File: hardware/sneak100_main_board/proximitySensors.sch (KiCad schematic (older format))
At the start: 4 parts, among them J11 Conn_01x03, J12 Conn_01x03, J13 Conn_01x03, J14 Conn_01x03

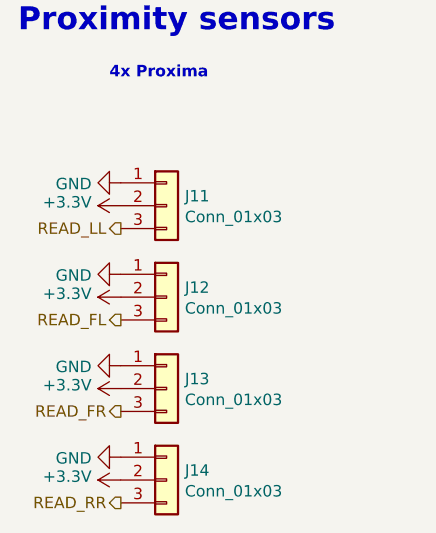
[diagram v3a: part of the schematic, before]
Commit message: proximity sensors connectors
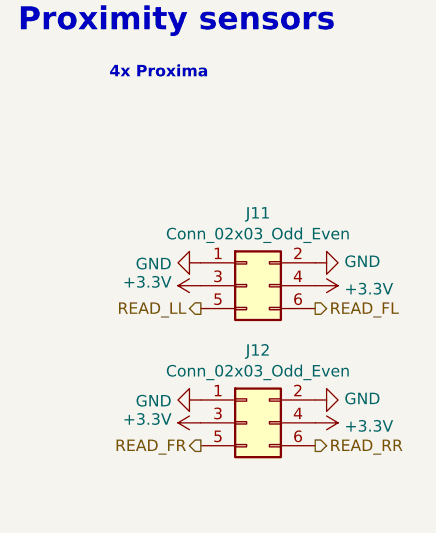
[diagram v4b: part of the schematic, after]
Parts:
- removed J11, J12, J13, J14: Conn_01x03, Connector_PinHeader_2.54mm:PinHeader_1x03_P2.54mm_Vertical, symbol Connector_Generic:Conn_01x03
- added J11, J12: Conn_02x03_Odd_Even, Connector_PinSocket_2.54mm:PinSocket_2x03_P2.54mm_Horizontal, symbol Connector_Generic:Conn_02x03_Odd_Even
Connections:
- net +3V3: now also J11.3 (Pin_3), J11.4 (Pin_4), J12.3 (Pin_3), J12.4 (Pin_4)
- net GND: now also J11.1 (Pin_1), J11.2 (Pin_2), J12.1 (Pin_1), J12.2 (Pin_2)
- net READ_FL: now also J11.6 (Pin_6)
- net READ_FR: now also J12.5 (Pin_5)
- net READ_LL: now also J11.5 (Pin_5)
- net READ_RR: now also J12.6 (Pin_6)
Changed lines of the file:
@@
 $EndDescr
-$Comp
-L Connector_Generic:Conn_01x03 J?
-U 1 1 610BA2A4
-P 5050 3200
-AR Path="/60E04A74/610BA2A4" Ref="J?"  Part="1"
-AR Path="/60E049FE/610BA2A4" Ref="J11"  Part="1"
-F 0 "J11" H 5130 3242 50  0000 L CNN
-F 1 "Conn_01x03" H 5130 3151 50  0000 L CNN
-F 2 "Connector_PinHeader_2.54mm:PinHeader_1x03_P2.54mm_Vertical" H 5050 3200 50  0001 C CNN
-F 3 "~" H 5050 3200 50  0001 C CNN
-	1    5050 3200
-	1    0    0    -1
-$EndComp
-$Comp
-L Connector_Generic:Conn_01x03 J?
-U 1 1 610BA2AA
-P 5050 3600
-AR Path="/60E04A74/610BA2AA" Ref="J?"  Part="1"
-AR Path="/60E049FE/610BA2AA" Ref="J12"  Part="1"
-F 0 "J12" H 5130 3642 50  0000 L CNN
-F 1 "Conn_01x03" H 5130 3551 50  0000 L CNN
-F 2 "Connector_PinHeader_2.54mm:PinHeader_1x03_P2.54mm_Vertical" H 5050 3600 50  0001 C CNN
-F 3 "~" H 5050 3600 50  0001 C CNN
-	1    5050 3600
-	1    0    0    -1
-$EndComp
-$Comp
-L Connector_Generic:Conn_01x03 J?
-U 1 1 610BA2B0
-P 5050 4000
-AR Path="/60E04A74/610BA2B0" Ref="J?"  Part="1"
-AR Path="/60E049FE/610BA2B0" Ref="J13"  Part="1"
-F 0 "J13" H 5130 4042 50  0000 L CNN
-F 1 "Conn_01x03" H 5130 3951 50  0000 L CNN
-F 2 "Connector_PinHeader_2.54mm:PinHeader_1x03_P2.54mm_Vertical" H 5050 4000 50  0001 C CNN
-F 3 "~" H 5050 4000 50  0001 C CNN
-	1    5050 4000
-	1    0    0    -1
-$EndComp
-$Comp
-L Connector_Generic:Conn_01x03 J?
-U 1 1 610BA2B6
-P 5050 4400
-AR Path="/60E04A74/610BA2B6" Ref="J?"  Part="1"
-AR Path="/60E049FE/610BA2B6" Ref="J14"  Part="1"
-F 0 "J14" H 5130 4442 50  0000 L CNN
-F 1 "Conn_01x03" H 5130 4351 50  0000 L CNN
-F 2 "Connector_PinHeader_2.54mm:PinHeader_1x03_P2.54mm_Vertical" H 5050 4400 50  0001 C CNN
-F 3 "~" H 5050 4400 50  0001 C CNN
-	1    5050 4400
-	1    0    0    -1
-$EndComp
 $Comp
 L power:+3.3V #PWR?
 U 1 1 610BA2BC
-P 4850 3200
+P 5200 3550
 AR Path="/60E04A74/610BA2BC" Ref="#PWR?"  Part="1"
-AR Path="/60E049FE/610BA2BC" Ref="#PWR080"  Part="1"
-F 0 "#PWR080" H 4850 3050 50  0001 C CNN
-F 1 "+3.3V" V 4865 3328 50  0000 L CNN
-F 2 "" H 4850 3200 50  0001 C CNN
-F 3 "" H 4850 3200 50  0001 C CNN
-	1    4850 3200
+AR Path="/60E049FE/610BA2BC" Ref="#PWR081"  Part="1"
+F 0 "#PWR081" H 5200 3400 50  0001 C CNN
+F 1 "+3.3V" V 5215 3678 50  0000 L CNN
+F 2 "" H 5200 3550 50  0001 C CNN
+F 3 "" H 5200 3550 50  0001 C CNN
+	1    5200 3550
 	0    -1   -1   0
 $EndComp
@@
 L power:+3.3V #PWR?
 U 1 1 610BA2C2
-P 4850 3600
+P 5700 3550
 AR Path="/60E04A74/610BA2C2" Ref="#PWR?"  Part="1"
 AR Path="/60E049FE/610BA2C2" Ref="#PWR082"  Part="1"
-F 0 "#PWR082" H 4850 3450 50  0001 C CNN
-F 1 "+3.3V" V 4865 3728 50  0000 L CNN
-F 2 "" H 4850 3600 50  0001 C CNN
-F 3 "" H 4850 3600 50  0001 C CNN
-	1    4850 3600
-	0    -1   -1   0
+F 0 "#PWR082" H 5700 3400 50  0001 C CNN
+F 1 "+3.3V" V 5715 3678 50  0000 L CNN
+F 2 "" H 5700 3550 50  0001 C CNN
+F 3 "" H 5700 3550 50  0001 C CNN
+	1    5700 3550
+	0    1    1    0
 $EndComp
 $Comp
 L power:+3.3V #PWR?
 U 1 1 610BA2C8
-P 4850 4000
+P 5200 4150
 AR Path="/60E04A74/610BA2C8" Ref="#PWR?"  Part="1"
-AR Path="/60E049FE/610BA2C8" Ref="#PWR084"  Part="1"
-F 0 "#PWR084" H 4850 3850 50  0001 C CNN
-F 1 "+3.3V" V 4865 4128 50  0000 L CNN
-F 2 "" H 4850 4000 50  0001 C CNN
-F 3 "" H 4850 4000 50  0001 C CNN
-	1    4850 4000
+AR Path="/60E049FE/610BA2C8" Ref="#PWR085"  Part="1"
+F 0 "#PWR085" H 5200 4000 50  0001 C CNN
+F 1 "+3.3V" V 5215 4278 50  0000 L CNN
+F 2 "" H 5200 4150 50  0001 C CNN
+F 3 "" H 5200 4150 50  0001 C CNN
+	1    5200 4150
 	0    -1   -1   0
 $EndComp
@@
 L power:+3.3V #PWR?
 U 1 1 610BA2CE
-P 4850 4400
+P 5700 4150
 AR Path="/60E04A74/610BA2CE" Ref="#PWR?"  Part="1"
 AR Path="/60E049FE/610BA2CE" Ref="#PWR086"  Part="1"
-F 0 "#PWR086" H 4850 4250 50  0001 C CNN
-F 1 "+3.3V" V 4865 4528 50  0000 L CNN
-F 2 "" H 4850 4400 50  0001 C CNN
-F 3 "" H 4850 4400 50  0001 C CNN
-	1    4850 4400
+F 0 "#PWR086" H 5700 4000 50  0001 C CNN
+F 1 "+3.3V" V 5715 4278 50  0000 L CNN
+F 2 "" H 5700 4150 50  0001 C CNN
+F 3 "" H 5700 4150 50  0001 C CNN
+	1    5700 4150
+	0    1    1    0
+$EndComp
+$Comp
+L power:GND #PWR?
+U 1 1 610BA2D4
+P 5700 4050
+AR Path="/60E04A74/610BA2D4" Ref="#PWR?"  Part="1"
+AR Path="/60E049FE/610BA2D4" Ref="#PWR084"  Part="1"
+F 0 "#PWR084" H 5700 3800 50  0001 C CNN
+F 1 "GND" V 5705 3922 50  0000 R CNN
+F 2 "" H 5700 4050 50  0001 C CNN
+F 3 "" H 5700 4050 50  0001 C CNN
+	1    5700 4050
 	0    -1   -1   0
 $EndComp
 $Comp
 L power:GND #PWR?
-U 1 1 610BA2D4
-P 4850 4300
-AR Path="/60E04A74/610BA2D4" Ref="#PWR?"  Part="1"
-AR Path="/60E049FE/610BA2D4" Ref="#PWR085"  Part="1"
-F 0 "#PWR085" H 4850 4050 50  0001 C CNN
-F 1 "GND" V 4855 4172 50  0000 R CNN
-F 2 "" H 4850 4300 50  0001 C CNN
-F 3 "" H 4850 4300 50  0001 C CNN
-	1    4850 4300
-	0    1    1    0
-$EndComp
-$Comp
-L power:GND #PWR?
 U 1 1 610BA2DA
-P 4850 3900
+P 5200 4050
 AR Path="/60E04A74/610BA2DA" Ref="#PWR?"  Part="1"
 AR Path="/60E049FE/610BA2DA" Ref="#PWR083"  Part="1"
-F 0 "#PWR083" H 4850 3650 50  0001 C CNN
-F 1 "GND" V 4855 3772 50  0000 R CNN
-F 2 "" H 4850 3900 50  0001 C CNN
-F 3 "" H 4850 3900 50  0001 C CNN
-	1    4850 3900
+F 0 "#PWR083" H 5200 3800 50  0001 C CNN
+F 1 "GND" V 5205 3922 50  0000 R CNN
+F 2 "" H 5200 4050 50  0001 C CNN
+F 3 "" H 5200 4050 50  0001 C CNN
+	1    5200 4050
 	0    1    1    0
 $EndComp
@@
 L power:GND #PWR?
 U 1 1 610BA2E0
-P 4850 3500
+P 5700 3450
 AR Path="/60E04A74/610BA2E0" Ref="#PWR?"  Part="1"
-AR Path="/60E049FE/610BA2E0" Ref="#PWR081"  Part="1"
-F 0 "#PWR081" H 4850 3250 50  0001 C CNN
-F 1 "GND" V 4855 3372 50  0000 R CNN
-F 2 "" H 4850 3500 50  0001 C CNN
-F 3 "" H 4850 3500 50  0001 C CNN
-	1    4850 3500
-	0    1    1    0
+AR Path="/60E049FE/610BA2E0" Ref="#PWR080"  Part="1"
+F 0 "#PWR080" H 5700 3200 50  0001 C CNN
+F 1 "GND" V 5705 3322 50  0000 R CNN
+F 2 "" H 5700 3450 50  0001 C CNN
+F 3 "" H 5700 3450 50  0001 C CNN
+	1    5700 3450
+	0    -1   -1   0
 $EndComp
 $Comp
 L power:GND #PWR?
 U 1 1 610BA2E6
-P 4850 3100
+P 5200 3450
 AR Path="/60E04A74/610BA2E6" Ref="#PWR?"  Part="1"
 AR Path="/60E049FE/610BA2E6" Ref="#PWR079"  Part="1"
-F 0 "#PWR079" H 4850 2850 50  0001 C CNN
-F 1 "GND" V 4855 2972 50  0000 R CNN
-F 2 "" H 4850 3100 50  0001 C CNN
-F 3 "" H 4850 3100 50  0001 C CNN
-	1    4850 3100
+F 0 "#PWR079" H 5200 3200 50  0001 C CNN
+F 1 "GND" V 5205 3322 50  0000 R CNN
+F 2 "" H 5200 3450 50  0001 C CNN
+F 3 "" H 5200 3450 50  0001 C CNN
+	1    5200 3450
 	0    1    1    0
 $EndComp
-Text HLabel 4850 3300 0    50   Output ~ 0
+Text HLabel 5200 3650 0    50   Output ~ 0
 READ_LL
-Text HLabel 4850 3700 0    50   Output ~ 0
+Text HLabel 5700 3650 2    50   Output ~ 0
 READ_FL
-Text HLabel 4850 4100 0    50   Output ~ 0
+Text HLabel 5200 4250 0    50   Output ~ 0
 READ_FR
-Text HLabel 4850 4500 0    50   Output ~ 0
+Text HLabel 5700 4250 2    50   Output ~ 0
 READ_RR
 Text Notes 4400 2450 0    100  ~ 20
@@
 Text Notes 4800 2650 0    50   ~ 10
 4x Proxima
+$Comp
+L Connector_Generic:Conn_02x03_Odd_Even J11
+U 1 1 6112C7F5
+P 5400 3550
+F 0 "J11" H 5450 3867 50  0000 C CNN
+F 1 "Conn_02x03_Odd_Even" H 5450 3776 50  0000 C CNN
+F 2 "Connector_PinSocket_2.54mm:PinSocket_2x03_P2.54mm_Horizontal" H 5400 3550 50  0001 C CNN
+F 3 "~" H 5400 3550 50  0001 C CNN
+	1    5400 3550
+	1    0    0    -1
+$EndComp
+$Comp
+L Connector_Generic:Conn_02x03_Odd_Even J12
+U 1 1 6112D481
+P 5400 4150
+F 0 "J12" H 5450 4467 50  0000 C CNN
+F 1 "Conn_02x03_Odd_Even" H 5450 4376 50  0000 C CNN
+F 2 "Connector_PinSocket_2.54mm:PinSocket_2x03_P2.54mm_Horizontal" H 5400 4150 50  0001 C CNN
+F 3 "~" H 5400 4150 50  0001 C CNN
+	1    5400 4150
+	1    0    0    -1
+$EndComp
 $EndSCHEMATC

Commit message: Silk layer text
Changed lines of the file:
@@
 Text HLabel 5700 4250 2    50   Output ~ 0
 READ_RR
-Text Notes 4400 2450 0    100  ~ 20
+Text Notes 4800 2750 0    100  ~ 20
 Proximity sensors
-Text Notes 4800 2650 0    50   ~ 10
+Text Notes 5200 2950 0    50   ~ 10
 4x Proxima
 $Comp
